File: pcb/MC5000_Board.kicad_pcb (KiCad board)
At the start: 2 copper layers, 100 x 97.5 mm, 125 parts, among them J1 USB_B_Micro, J10 Conn_01x04_Male, J11 Conn_01x04_Male, J12 Conn_01x04_Male, J13 Conn_01x04_Male, J14 Conn_01x04_Female, J15 Conn_01x04_Female, J16 Conn_01x04_Female, J17 Conn_01x04_Female, J18 Conn_01x04_Female, J19 Conn_01x04_Female, J2 Conn_01x04_Male, J20 Conn_01x04_Female, J21 Conn_01x04_Female, J22 Conn_01x04_Female, J23 Conn_01x04_Female, J3 Conn_01x04_Male, J4 Conn_01x04_Male, J5 Conn_01x04_Male, J6 Conn_01x04_Male, J7 Conn_01x04_Male, J8 Conn_01x04_Male, J9 Conn_01x04_Male, Q1 S9013, Q2 S9013, Q3 S9013, Q4 S9013, SW1 SW_MEC_5E, SW2 SW_MEC_5E, U1 PFS173-S08, U2 PFS173-S08, U3 PFS173-S08, U4 PFS173-S08, U5 CH340K, U6 PFS173-S08, U7 PFS173-S08, U8 PCA9555PW

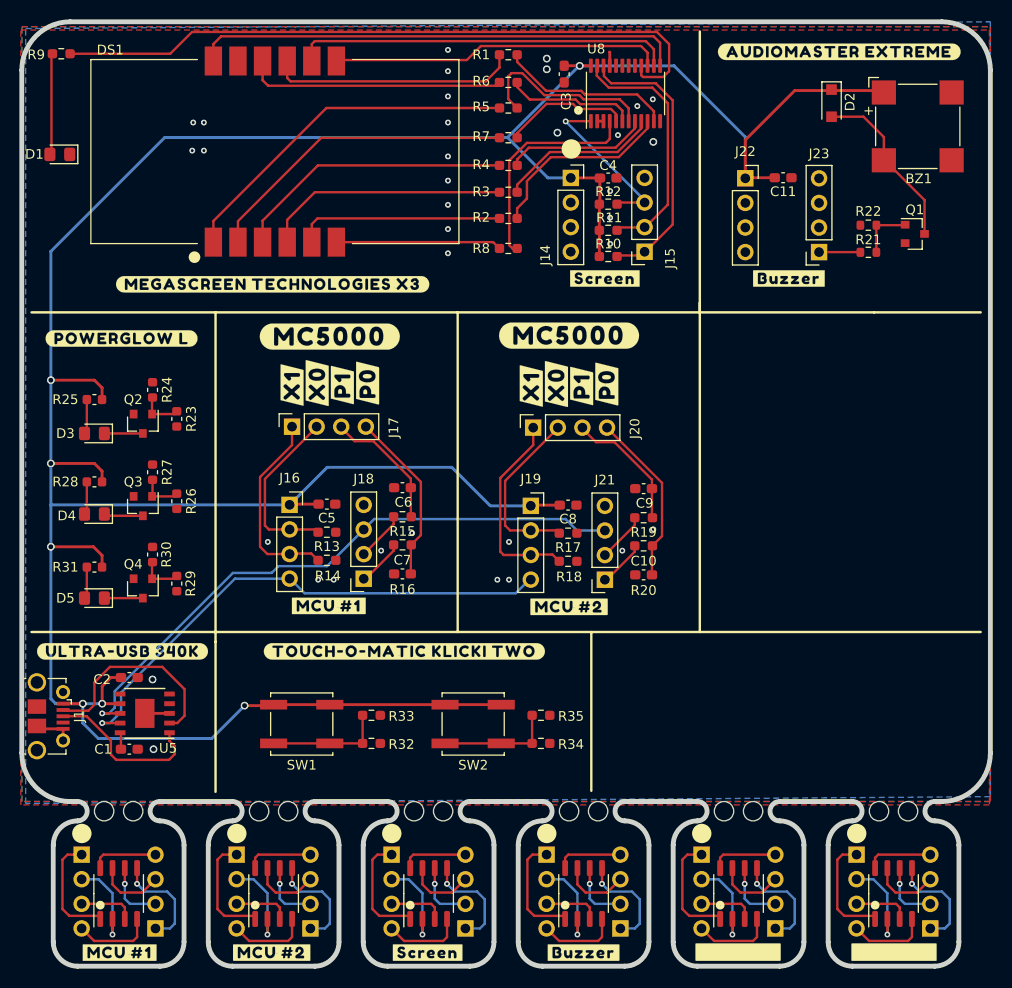
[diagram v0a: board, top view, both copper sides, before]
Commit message: changed pcb file structure
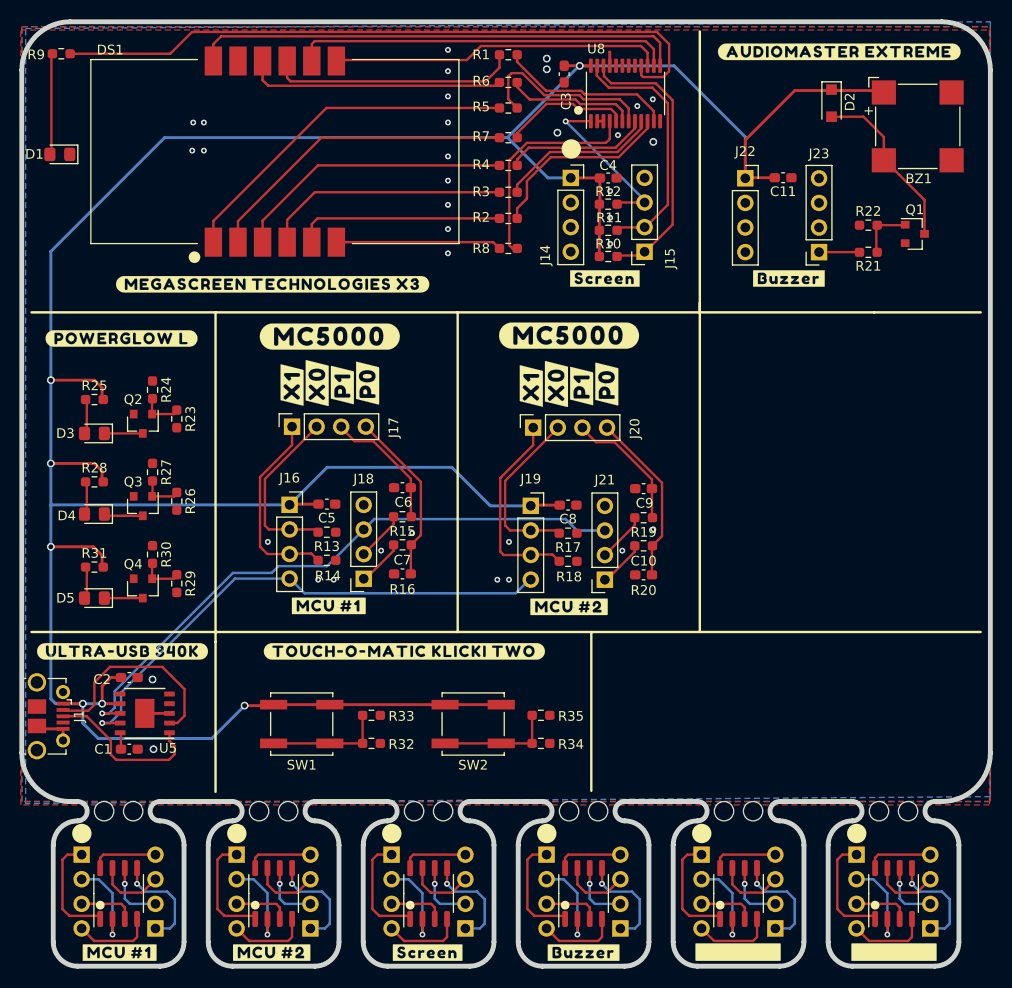
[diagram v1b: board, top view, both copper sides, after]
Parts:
- R21, R22, R23, R24, R25, R26, R27, R28, R29, R30, R31: footprint Resistor_SMD:R_0603_1608Metric -> Resistor_SMD:R_0603_1608Metric_Pad0.98x0.95mm_HandSolder

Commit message: finished pcb
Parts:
- removed the ? at (89.5, 105.0)
- removed the ? at (107.8, 77.6)
- removed the ? at (106.5, 72.4)
- removed the ? at (110.2, 66.5)
- removed the ? at (81.8, 72.5)
- removed the ? at (91.9, 136.1)
- removed the ? at (108.0, 136.1)
- removed the ? at (60.4, 105.0)
- removed the ? at (60.3, 72.7)
- removed the ? at (129.2, 66.5)
- removed the ? at (106.5, 100.4)
- removed the ? at (81.7, 100.3)
- removed the ? at (110.4, 77.4)
- removed the ? at (105.2, 77.4)
- removed the ? at (102.6, 77.6)
- removed Q2, Q3, Q4: S9013, Package_TO_SOT_SMD:SOT-23
- removed R27, R30: 100K, Resistor_SMD:R_0603_1608Metric_Pad0.98x0.95mm_HandSolder
- removed R29: 200R, Resistor_SMD:R_0603_1608Metric_Pad0.98x0.95mm_HandSolder
- added ?: , buzzard_labels, F.Cu at (139.0, 105.3)
- added ?: , buzzard_labels, F.Cu at (122.0, 79.8)
- added ?: , buzzard_labels, F.Cu at (122.0, 94.6)
- added ?: , buzzard_labels, F.Cu at (136.6, 93.3)
- added ?: , buzzard_labels, F.Cu at (136.3, 90.8)
- added ?: , buzzard_labels, F.Cu at (91.9, 136.2)
- added ?: , buzzard_labels, F.Cu at (108.0, 136.2)
- added ?: , buzzard_labels, F.Cu at (106.7, 72.4)
- added ?: , buzzard_labels, F.Cu at (81.8, 72.3)
- added ?: , buzzard_labels, F.Cu at (95.8, 117.9)
- added ?: , buzzard_labels, F.Cu at (80.6, 117.9)
- added ?: , buzzard_labels, F.Cu at (117.2, 105.3)
- added ?: , buzzard_labels, F.Cu at (88.2, 105.3)
- added ?: , buzzard_labels, F.Cu at (60.3, 72.4)
- added ?: , buzzard_labels, F.Cu at (110.4, 76.4)
- added ?: , buzzard_labels, F.Cu at (105.2, 76.4)
- added ?: , buzzard_labels, F.Cu at (102.6, 76.6)
- added ?: , buzzard_labels, F.Cu at (107.8, 76.6)
- added ?: , buzzard_labels, F.Cu at (138.3, 82.0)
- added ?: , buzzard_labels, F.Cu at (137.0, 84.6)
- added ?: , buzzard_labels, F.Cu at (135.2, 79.4)
- added ?: , buzzard_labels, F.Cu at (135.1, 76.8)
- added ?: , buzzard_labels, F.Cu at (135.6, 74.2)
- added ?: , buzzard_labels, F.Cu at (133.6, 96.0)
- added ?: , buzzard_labels, F.Cu at (133.8, 98.5)
- added D6: SMD3528C-50, LED_SMD:LED_1210_3225Metric, F.Cu at (116.5, 112.0)
- added J24: Conn_01x04_Female, Connector_PinSocket_2.54mm:PinSocket_1x04_P2.54mm_Vertical, F.Cu at (125.2, 90.9)
- added J25: Conn_01x05_Female, Connector_PinSocket_2.54mm:PinSocket_1x05_P2.54mm_Vertical, F.Cu at (125.2, 74.3)
- R23: value 200R -> 100K
- R24: value 100K -> NTC - 100k
- R26: value 200R -> 10K
- moved R24 83.4 mm to (138.8, 113.9), turned to 0 degrees
- moved R23 78.9 mm to (138.8, 111.3), turned to 180 degrees
- moved R26 59.6 mm to (121.2, 112.0), turned to 180 degrees
- moved D3 3.45 mm to (60.5, 80.8)
- moved D5 3.45 mm to (60.5, 97.8)
- moved R25 3.45 mm to (60.5, 77.3)
- moved R28 3.45 mm to (60.5, 85.8)
- moved R31 3.45 mm to (60.5, 94.6)
- moved D4 3.45 mm to (60.5, 89.1)
- moved R35 2.22 mm to (101.8, 110.3), turned to 270 degrees
- moved R34 1.81 mm to (101.8, 114.7), turned to 90 degrees
- moved SW1 1.70 mm to (80.6, 112.5)
- moved R33 1.53 mm to (86.9, 110.3), turned to 270 degrees
- moved ? 1.00 mm to (85.7, 76.3)
- moved ? 1.00 mm to (83.1, 76.5)
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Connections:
- net Net-(Q2-Pad1) renamed TEMP_SENSOR
- D3 pad 1: Net-(D3-Pad1) -> LED_RED
- D4 pad 1: Net-(D4-Pad1) -> LED_YELLOW
- D5 pad 1: Net-(D5-Pad1) -> LED_GREEN
- J14 pad 3: XBUS_Display -> DISPLAY
- J22 pad 3: XBUS_Buzzer -> BUZZER
- R23 pad 2: LED_RED -> GND
- R24 pad 1: GND -> VCC
- R26 pad 1: Net-(Q3-Pad1) -> GND
- R26 pad 2: LED_YELLOW -> LIGHT_SENSOR
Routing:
- net LED_GREEN: track 0.00 -> 90.9 mm
- net LED_YELLOW: track 0.00 -> 82.4 mm
- net LED_RED: track 0.00 -> 72.6 mm
- net VCC: track 320.1 -> 373.5 mm
- net SWITCH_1: track 0.00 -> 46.1 mm
- net TEMP_SENSOR: track 4.40 -> 43.2 mm
- net DISPLAY: track 0.00 -> 34.4 mm
- net SWITCH_2: track 0.00 -> 33.9 mm
- net BUZZER: track 0.00 -> 21.7 mm
- net LIGHT_SENSOR: track 0.00 -> 20.7 mm
- net Net-(Q3-Pad1): track 4.40 -> 0.00 mm
- net Net-(Q4-Pad1): track 4.40 -> 0.00 mm
- net Net-(D4-Pad1): track 4.05 -> 0.00 mm
- net Net-(D5-Pad1): track 3.98 -> 0.00 mm
- net Net-(D3-Pad1): track 3.98 -> 0.00 mm
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
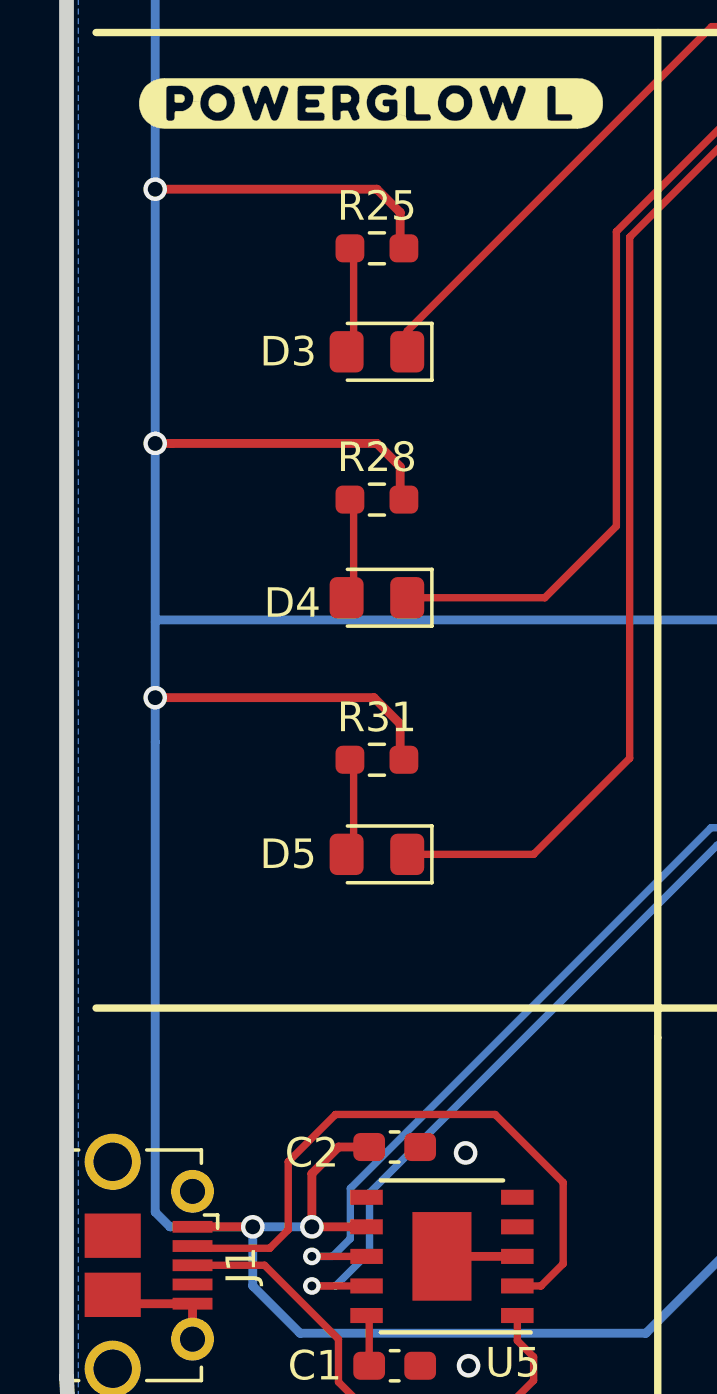
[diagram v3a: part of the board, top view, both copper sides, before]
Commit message: Connected LEDs to GND
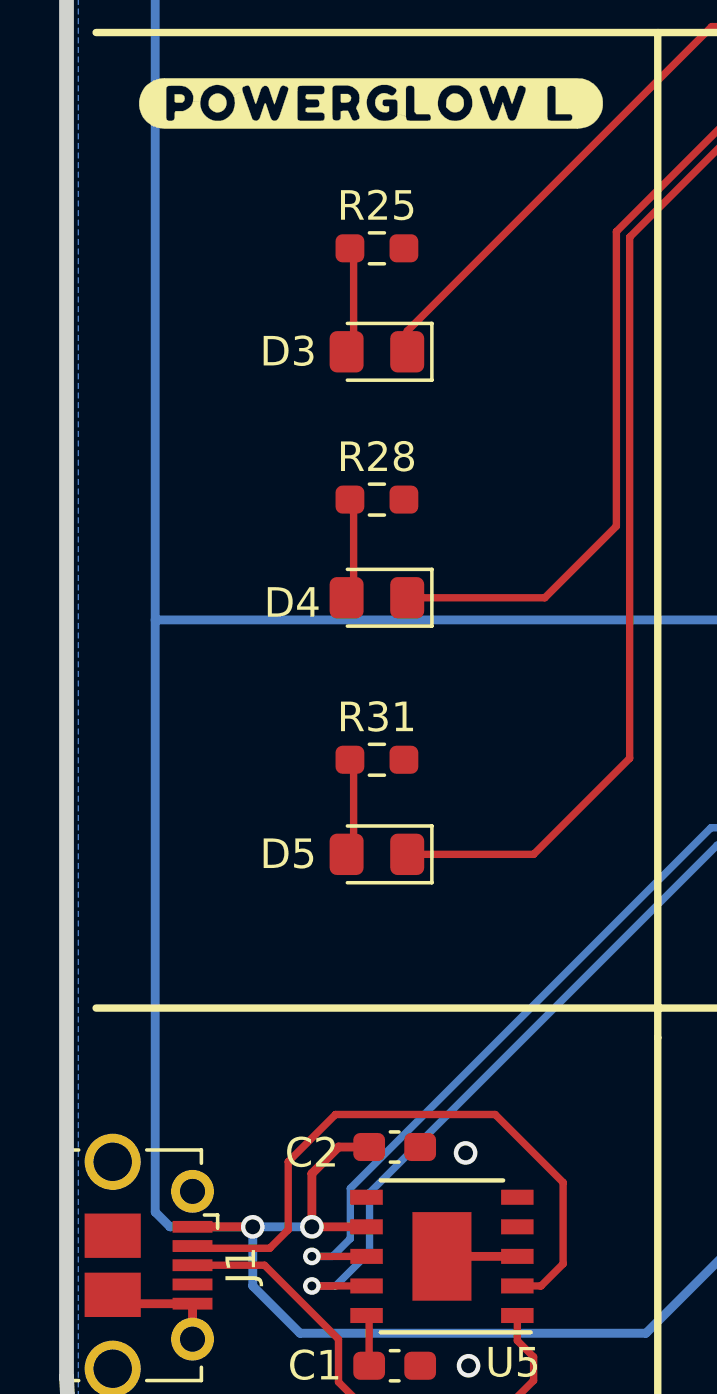
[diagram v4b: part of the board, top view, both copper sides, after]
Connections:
- R25 pad 2: VCC -> GND
- R28 pad 2: VCC -> GND
- R31 pad 2: VCC -> GND
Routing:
- net VCC: track 373.5 -> 344.3 mm, vias 7 -> 4

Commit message: XBus changes; PCB changes
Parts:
- removed the ? at (91.9, 136.2)
- removed the ? at (108.0, 136.2)
- removed the ? at (75.8, 136.2)
- removed the ? at (60.1, 136.2)
- removed J10, J11, J12, J13, J2, J3, J4, J5, J6, J7, J8, J9: Conn_01x04_Male, Connector_PinHeader_2.54mm:PinHeader_1x04_P2.54mm_Vertical
- removed the REF** at (141.5, 121.5)
- removed the REF** at (74.5, 121.5)
- removed the REF** at (61.5, 121.5)
- removed the REF** at (58.5, 121.5)
- removed the REF** at (138.5, 121.5)
- removed the REF** at (125.5, 121.5)
- removed the REF** at (122.5, 121.5)
- removed the REF** at (109.5, 121.5)
- removed the REF** at (106.5, 121.5)
- removed the REF** at (93.5, 121.5)
- removed the REF** at (90.5, 121.5)
- removed the REF** at (77.5, 121.5)
- removed U1, U2, U3, U4, U6, U7: PFS173-S08, Package_SO:SOP-8_3.9x4.9mm_P1.27mm
- added R12: 1M, Resistor_SMD:R_0603_1608Metric_Pad0.98x0.95mm_HandSolder, F.Cu at (128.6, 59.0)
- added R27: 1M, Resistor_SMD:R_0603_1608Metric_Pad0.98x0.95mm_HandSolder, F.Cu at (110.6, 67.2)
- added REF**: JLC_assembly_hole, LCSC_parts:JLC_assembly_hole, F.Cu at (52.5, 42.5)
- added REF**: JLC_assembly_hole, LCSC_parts:JLC_assembly_hole, F.Cu at (146.5, 117.3)
- added REF**: JLC_assembly_hole, LCSC_parts:JLC_assembly_hole, F.Cu at (53.0, 117.9)
- DS1: value SLS0563DRA1GD -> SLR0523DYA1BD; footprint LCSC_parts:SLS0563DRA1GD -> LCSC_parts:SLR0523DYA1BD
- Q1: footprint Package_TO_SOT_SMD:SOT-23 -> LCSC_parts:SOT-23_rotated
- R1, R2, R21, R25, R28, R3, R33, R35, R4, R5, R6, R7, R8: value 200R -> 220R
- R31: value 200R -> 120R
- R9: value 200R -> 2K2
- U5: value CH340K -> CH340E; footprint LCSC_parts:ESSOP-10_3.9x4.9mm_P1.00mm -> Package_SO:MSOP-10_3x3mm_P0.5mm
- moved R2 14.1 mm to (100.2, 46.2)
- moved R3 5.90 mm to (100.2, 63.5)
- moved R9 5.20 mm to (54.0, 48.5)
- moved R5 3.05 mm to (100.3, 52.0)
- moved R4 2.90 mm to (100.3, 57.7)
- moved R7 2.90 mm to (100.3, 54.9)
- moved R6 2.85 mm to (100.3, 49.1)
- moved R8 2.75 mm to (100.2, 60.6)
- moved ? 1.53 mm to (76.3, 66.2)
- moved DS1 1.21 mm to (76.2, 54.6)
- moved U5 0.86 mm to (63.4, 110.9)
- moved Q1 0.09 mm to (142.1, 62.0), turned to 180 degrees
- turned D3 to 0 degrees
- turned D4 to 0 degrees
- turned D5 to 0 degrees
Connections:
- D3 pad 1: LED_RED -> Net-(D3-Pad1)
- D3 pad 2: Net-(D3-Pad2) -> LED_RED
- D4 pad 1: LED_YELLOW -> Net-(D4-Pad1)
- D4 pad 2: Net-(D4-Pad2) -> LED_YELLOW
- D5 pad 1: LED_GREEN -> Net-(D5-Pad1)
- D5 pad 2: Net-(D5-Pad2) -> LED_GREEN
- DS1 pad 11: (no net) -> Net-(DS1-Pad11)
- DS1 pad 6: Net-(DS1-Pad6) -> (no net)
- R1 pad 1: Net-(DS1-Pad9) -> Net-(DS1-Pad11)
- R2 pad 1: Net-(DS1-Pad5) -> Net-(DS1-Pad7)
- R25 pad 1: Net-(D3-Pad2) -> Net-(D3-Pad1)
- R28 pad 1: Net-(D4-Pad2) -> Net-(D4-Pad1)
- R31 pad 1: Net-(D5-Pad2) -> Net-(D5-Pad1)
- R4 pad 1: Net-(DS1-Pad3) -> Net-(DS1-Pad2)
- R7 pad 1: Net-(DS1-Pad2) -> Net-(DS1-Pad5)
- R8 pad 1: Net-(DS1-Pad6) -> Net-(DS1-Pad3)
- U8 pad 14: Net-(DS1-Pad8) -> Net-(DS1-Pad9)
- U8 pad 15: Net-(DS1-Pad7) -> Net-(DS1-Pad8)
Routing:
- net Net-(DS1-Pad11): track 0.00 -> 31.2 mm
- net Net-(DS1-Pad5): track 21.5 -> 45.6 mm
- net Net-(DS1-Pad9): track 25.7 -> 44.1 mm
- net Net-(DS1-Pad7): track 34.4 -> 17.3 mm
- net Net-(DS1-Pad6): track 17.1 -> 0.00 mm
- net Net-(J12-Pad1): track 11.8 -> 0.00 mm
- net Net-(J8-Pad1): track 11.8 -> 0.00 mm
- net Net-(J6-Pad1): track 11.8 -> 0.00 mm
- net Net-(J2-Pad1): track 11.8 -> 0.00 mm
- net Net-(J10-Pad1): track 11.8 -> 0.00 mm
- net Net-(J4-Pad1): track 11.8 -> 0.00 mm
- net LED_YELLOW: track 82.4 -> 94.0 mm
- net Net-(J11-Pad1): track 11.0 -> 0.00 mm, vias 1 -> 0
- net Net-(J5-Pad1): track 11.0 -> 0.00 mm, vias 1 -> 0
- net Net-(J13-Pad1): track 11.0 -> 0.00 mm, vias 1 -> 0
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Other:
- board size 100 x 97.5 mm -> 100 x 80.5 mm

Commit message: Production board
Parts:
- removed J14, J15, J16, J18, J19, J21, J22, J23: Conn_01x04_Female, Connector_PinSocket_2.54mm:PinSocket_1x04_P2.54mm_Vertical
- added U1: PFS173-S08, Package_SO:SOP-8_3.9x4.9mm_P1.27mm, F.Cu at (109.8, 61.3)
- added U2: PFS173-S08, Package_SO:SOP-8_3.9x4.9mm_P1.27mm, F.Cu at (82.3, 91.9)
- added U3: PFS173-S08, Package_SO:SOP-8_3.9x4.9mm_P1.27mm, F.Cu at (107.2, 91.9)
- added U4: PFS173-S08, Package_SO:SOP-8_3.9x4.9mm_P1.27mm, F.Cu at (128.1, 61.9)
- J17, J20, J24: footprint Connector_PinSocket_2.54mm:PinSocket_1x04_P2.54mm_Vertical -> LCSC_parts:PinSocket_1x04_P2.54mm_Vertical_centered
- J25: footprint Connector_PinSocket_2.54mm:PinSocket_1x05_P2.54mm_Vertical -> LCSC_parts:PinSocket_1x05_P2.54mm_Vertical_centered
- moved R14 7.18 mm to (74.5, 91.3), turned to 0 degrees
- moved R18 7.16 mm to (99.4, 91.3), turned to 0 degrees
- moved R12 7.10 mm to (127.9, 66.1)
- moved R13 7.10 mm to (74.5, 94.2), turned to 180 degrees
- moved C4 7.09 mm to (104.9, 60.4), turned to 270 degrees
- moved R17 7.08 mm to (99.5, 94.2), turned to 180 degrees
- moved R11 6.87 mm to (117.3, 60.5), turned to 0 degrees
- moved R27 6.87 mm to (117.4, 66.3)
- moved R10 6.87 mm to (117.4, 63.4)
- moved R12 6.85 mm to (117.3, 57.8), turned to 0 degrees
- moved J25 4.90 mm to (125.2, 79.2), turned to 270 degrees
- moved J20 3.86 mm to (106.7, 80.9), turned to 0 degrees
- moved J24 3.85 mm to (125.2, 94.8), turned to 270 degrees
- moved J17 3.82 mm to (81.7, 80.9), turned to 0 degrees
- moved C11 2.72 mm to (126.6, 58.0)
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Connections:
- C4 pad 1: GND -> VCC
- C4 pad 2: VCC -> GND
- D6 pad 1: LIGHT_SENSOR -> VCC
- D6 pad 2: VCC -> LIGHT_SENSOR
- U8 pad 1: Net-(J15-Pad3) -> Net-(U1-Pad7)
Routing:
- net VCC: track 334.0 -> 356.7 mm, vias 4 -> 9
- net Net-(J15-Pad3): track 18.1 -> 0.00 mm, vias 1 -> 0
- net Net-(U1-Pad7): track 0.00 -> 17.0 mm, vias 0 -> 2
- net DISPLAY: track 35.8 -> 25.2 mm
- net RXD: track 56.1 -> 65.4 mm, vias 1 -> 3
- net BUZZER: track 21.1 -> 16.3 mm
- net Net-(R10-Pad2): track 29.7 -> 33.0 mm
- net Net-(J17-Pad2): track 19.2 -> 21.4 mm
- net Net-(J20-Pad2): track 19.3 -> 21.4 mm
- net Net-(R21-Pad2): track 4.27 -> 5.80 mm
- net Net-(R16-Pad2): track 4.90 -> 3.59 mm
- net Net-(R20-Pad2): track 4.90 -> 3.59 mm
- net Net-(J20-Pad1): track 21.5 -> 20.4 mm
- net TXD: track 64.8 -> 65.9 mm, vias 1 -> 3
- net Net-(J17-Pad1): track 21.4 -> 20.4 mm
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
